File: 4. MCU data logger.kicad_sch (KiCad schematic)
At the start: 25 parts, among them U1 24LC1025, U2 24LC1025, U4 ATMEGA328P-AU, U5 DS1337S_, Y1 32.768 KHz, Y2 16 MHz

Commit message: Completed 2layer project
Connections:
- net VCC: now also BT1.1 (+), C2.1, D2.2 (A), U4.18 (AVCC), U4.4 (VCC)
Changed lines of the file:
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@@
+	)
+	(label "VCC"
+		(at 266.7 29.21 0)
+		(fields_autoplaced yes)
+		(effects
+			(font
+				(size 1.27 1.27)
+			)
+			(justify left bottom)
+		)
+		(property "Netclass" "Power"
+			(at 266.7 30.48 0)
+			(effects
+				(font
+					(size 1.27 1.27)
+					(italic yes)
+				)
+				(justify left)
+				(hide yes)
+			)
+		)
 	)
 	(label "VCC"

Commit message: Fixed a defect
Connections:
- net SCK: no longer R3.2, U1.6 (SCL), U2.6 (SCL), U4.28 (PC5), U5.6 (SCL)
- new net SCL: R3.2, U1.6 (SCL), U2.6 (SCL), U4.28 (PC5), U5.6 (SCL)
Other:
- sheet Connectors ports: added SCL; removed none
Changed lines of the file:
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@@
 		)
 	)
-	(label "SCK"
+	(label "SCL"
 		(at 90.17 135.89 0)
 		(effects
@@
 		)
 	)
+	(label "SCK"
+		(at 184.15 140.97 180)
+		(effects
+			(font
+				(size 1.27 1.27)
+			)
+			(justify right bottom)
+		)
+	)
 	(label "RX"
 		(at 184.15 132.08 180)
@@
 		)
 	)
-	(label "SCK"
+	(label "SCL"
 		(at 101.6 138.43 270)
 		(effects
@@
 		)
 	)
-	(label "SCK"
+	(label "SCL"
 		(at 184.15 135.89 180)
 		(effects
@@
 		)
 	)
-	(label "SCK"
+	(label "SCL"
 		(at 45.72 54.61 180)
 		(effects
@@
 		)
 	)
-	(label "SCK"
+	(label "SCL"
 		(at 193.04 72.39 180)
 		(effects
@@
 		)
 	)
-	(label "SCK"
+	(label "SCL"
 		(at 58.42 135.89 0)
 		(effects
@@
 	)
 	(symbol
-		(lib_id "power:PWR_FLAG")
-		(at 48.26 127 0)
-		(unit 1)
-		(exclude_from_sim no)
-		(in_bom yes)
-		(on_board yes)
-		(dnp no)
-		(property "Reference" "#FLG03"
-			(at 48.26 125.095 0)
-			(effects
-				(font
-					(size 1.27 1.27)
-				)
-				(hide yes)
-			)
-		)
-		(property "Value" "PWR_FLAG"
-			(at 48.26 121.92 0)
-			(effects
-				(font
-					(size 1.27 1.27)
-				)
-			)
-		)
-		(property "Footprint" ""
-			(at 48.26 127 0)
-			(effects
-				(font
-					(size 1.27 1.27)
-				)
-				(hide yes)
-			)
-		)
-		(property "Datasheet" "~"
-			(at 48.26 127 0)
-			(effects
-				(font
-					(size 1.27 1.27)
-				)
-				(hide yes)
-			)
-		)
-		(property "Description" "Special symbol for telling ERC where power comes from"
-			(at 48.26 127 0)
-			(effects
-				(font
-					(size 1.27 1.27)
-				)
-				(hide yes)
-			)
-		)
-		(pin "1"
-		)
-		(instances
-			(project "4. MCU data logger"
-				(path "/e489fbc6-d144-4dc0-8ba8-45f2d374cc9b"
-					(reference "#FLG03")
-					(unit 1)
-				)
-			)
-		)
-	)
-	(symbol
 		(lib_id "Memory_EEPROM:24LC1025")
 		(at 48.26 135.89 0)
@@
 			)
 		)
-		(pin "SCK" bidirectional
-			(at 184.15 135.89 180)
-			(effects
-				(font
-					(size 1.27 1.27)
-				)
-				(justify left)
-			)
-		)
 		(pin "D4" bidirectional
 			(at 208.28 130.81 0)
@@
 			)
 		)
+		(pin "SCK" bidirectional
+			(at 184.15 140.97 180)
+			(effects
+				(font
+					(size 1.27 1.27)
+				)
+				(justify left)
+			)
+		)
+		(pin "SCL" bidirectional
+			(at 184.15 135.89 180)
+			(effects
+				(font
+					(size 1.27 1.27)
+				)
+				(justify left)
+			)
+		)

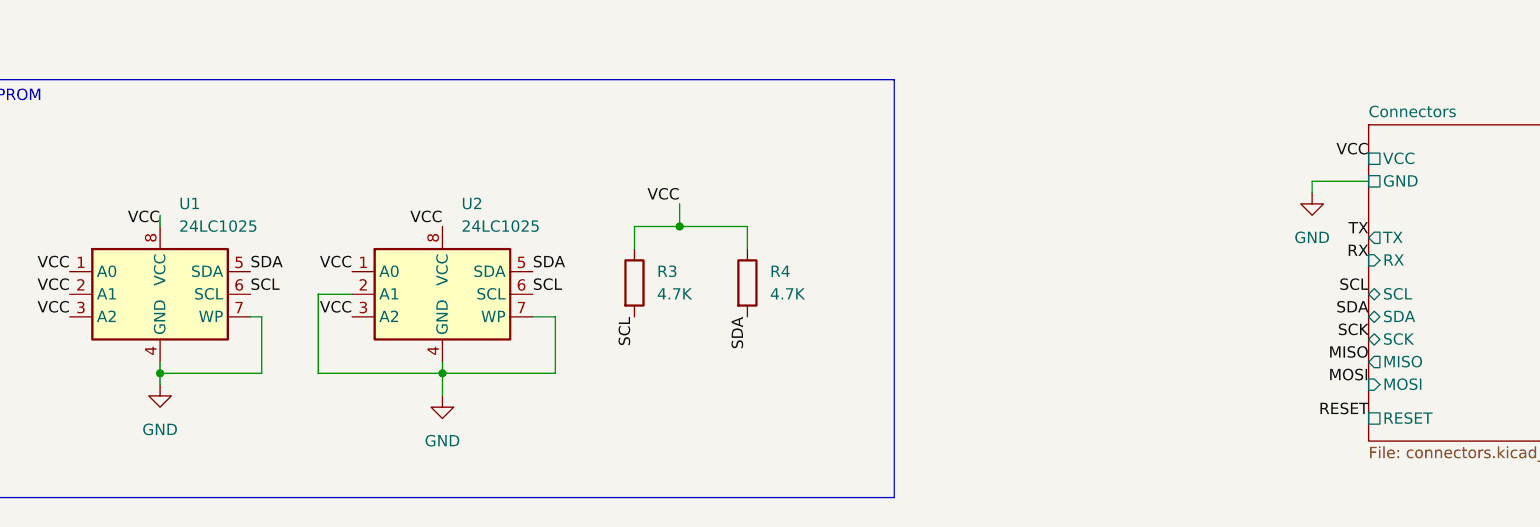
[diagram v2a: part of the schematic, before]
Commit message: Fixed defects in schematic
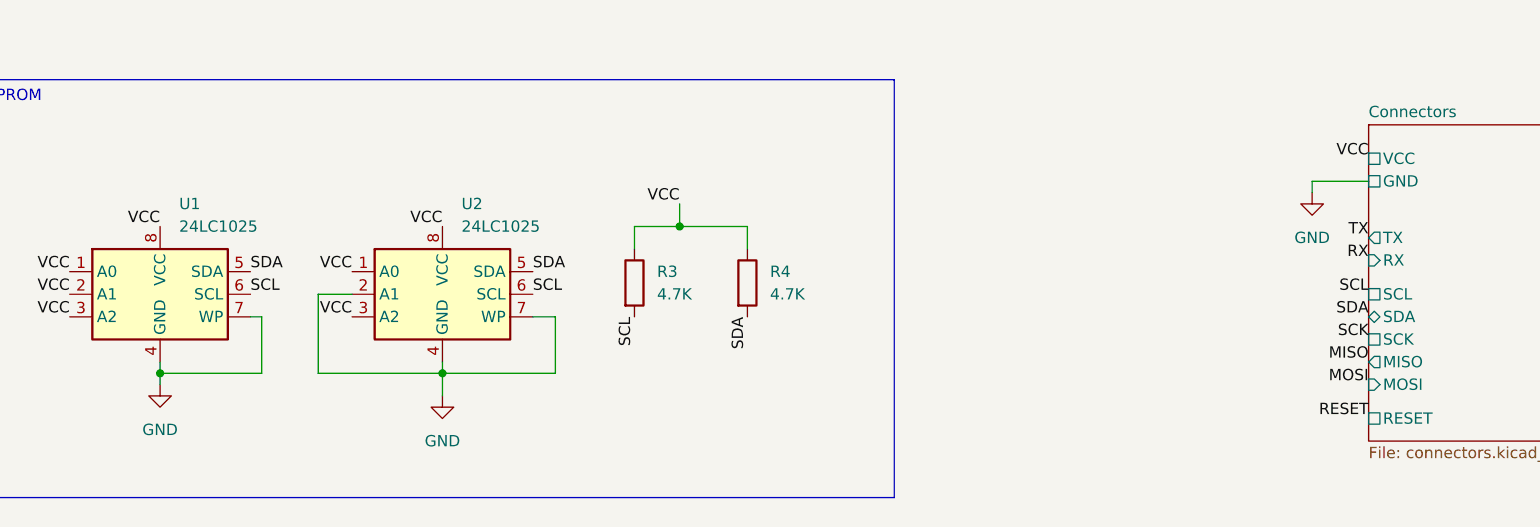
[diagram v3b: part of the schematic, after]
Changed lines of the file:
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@@
 	(wire
 		(pts
-			(xy 48.26 127) (xy 48.26 128.27)
-		)
-		(stroke
-			(width 0)
-			(type default)
-		)
-	)
-	(wire
-		(pts
 			(xy 48.26 143.51) (xy 48.26 144.78)
 		)
@@
 			)
 		)
-		(pin "SCK" bidirectional
-			(at 184.15 140.97 180)
+		(pin "SCL" passive
+			(at 184.15 135.89 180)
 			(effects
 				(font
@@
 			)
 		)
-		(pin "SCL" bidirectional
-			(at 184.15 135.89 180)
+		(pin "SCK" passive
+			(at 184.15 140.97 180)
 			(effects
 				(font
